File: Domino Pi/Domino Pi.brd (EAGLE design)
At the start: 71.1 x 33 mm, 77 parts, among them J1 MH28-1, J2 MH28-1, M1 DOMINO, SW1 IT-1210, U1 MP65151DJ, U2 MP2162GQH, U3 CP2104-F03-GM, U4 74LVC1G125DCK

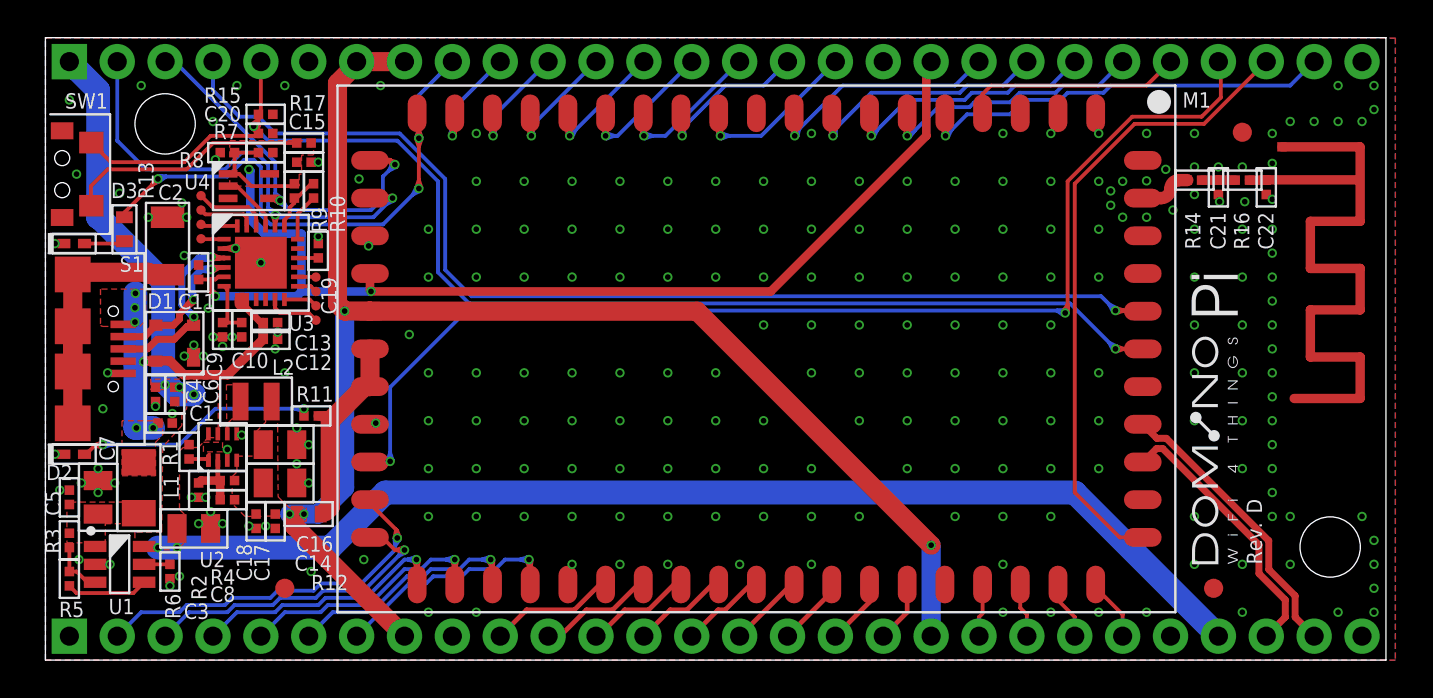
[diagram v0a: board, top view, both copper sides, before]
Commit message: Domnio Pi Rev. E: changed silkscreen font ratio to 20%
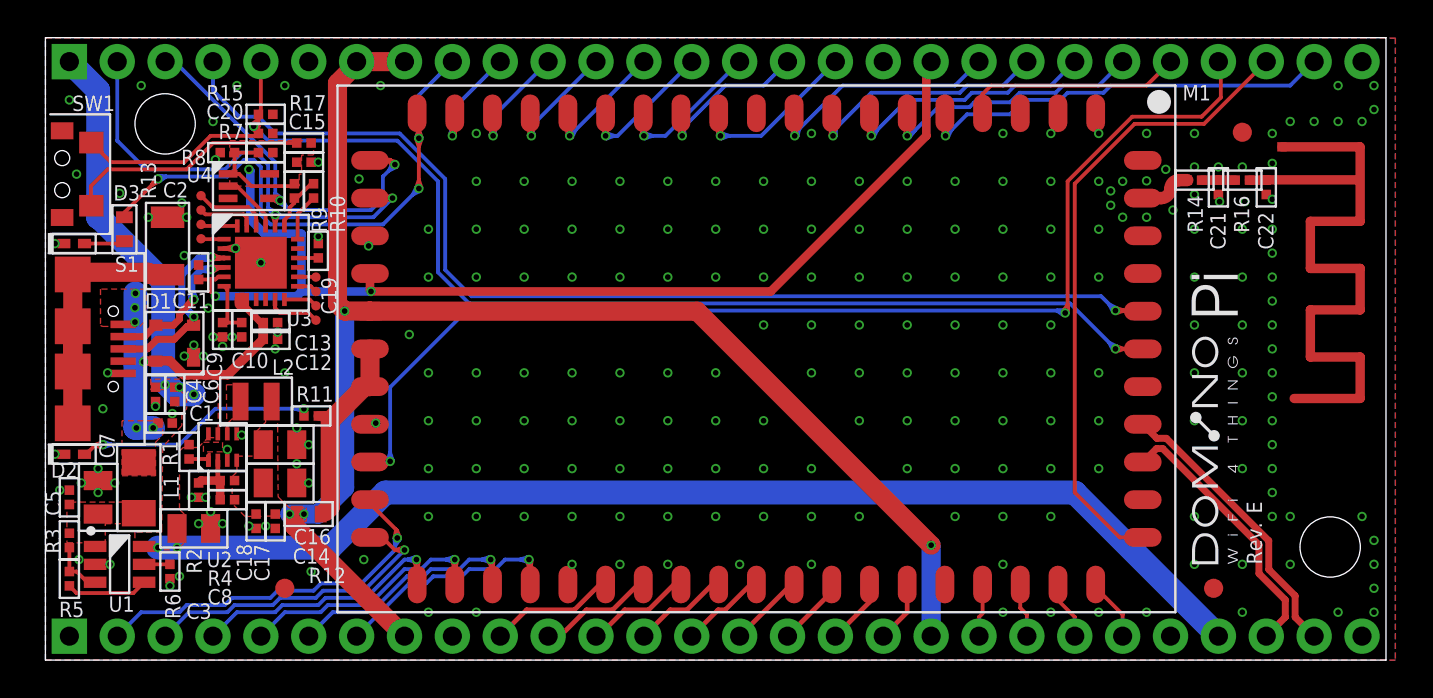
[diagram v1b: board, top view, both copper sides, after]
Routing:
- net +2V5: track 58.7 -> 57.6 mm
- net I2S_MICIN: track 19.0 -> 17.8 mm
- net UART_TX: track 30.5 -> 29.4 mm
